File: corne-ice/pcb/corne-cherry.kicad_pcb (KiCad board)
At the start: 2 copper layers, 275.5 x 105.6 mm, 118 parts, among them J1 MJ-4PP-9, J2 OLED, J3 MJ-4PP-9, J4 OLED, SW1 SW_PUSH, SW10 SW_PUSH, SW11 SW_PUSH, SW12 SW_PUSH, SW13 SW_PUSH, SW14 SW_PUSH, SW15 SW_PUSH, SW16 SW_PUSH, SW17 SW_PUSH, SW18 SW_PUSH, SW19 SW_PUSH, SW2 SW_PUSH, SW20 SW_PUSH, SW21 SW_PUSH, SW22 SW_PUSH, SW23 SW_PUSH, SW24 SW_PUSH, SW25 SW_PUSH, SW26 SW_PUSH, SW27 SW_PUSH, SW28 SW_PUSH, SW29 SW_PUSH, SW3 SW_PUSH, SW30 SW_PUSH, SW31 SW_PUSH, SW32 SW_PUSH, SW33 SW_PUSH, SW34 SW_PUSH, SW35 SW_PUSH, SW36 SW_PUSH, SW37 SW_PUSH, SW38 SW_PUSH, SW39 SW_PUSH, SW4 SW_PUSH, SW40 SW_PUSH, SW41 SW_PUSH, SW42 SW_PUSH, SW5 SW_PUSH, SW6 SW_PUSH, SW7 SW_PUSH, SW8 SW_PUSH, SW9 SW_PUSH, U1 ProMicro, U2 ProMicro

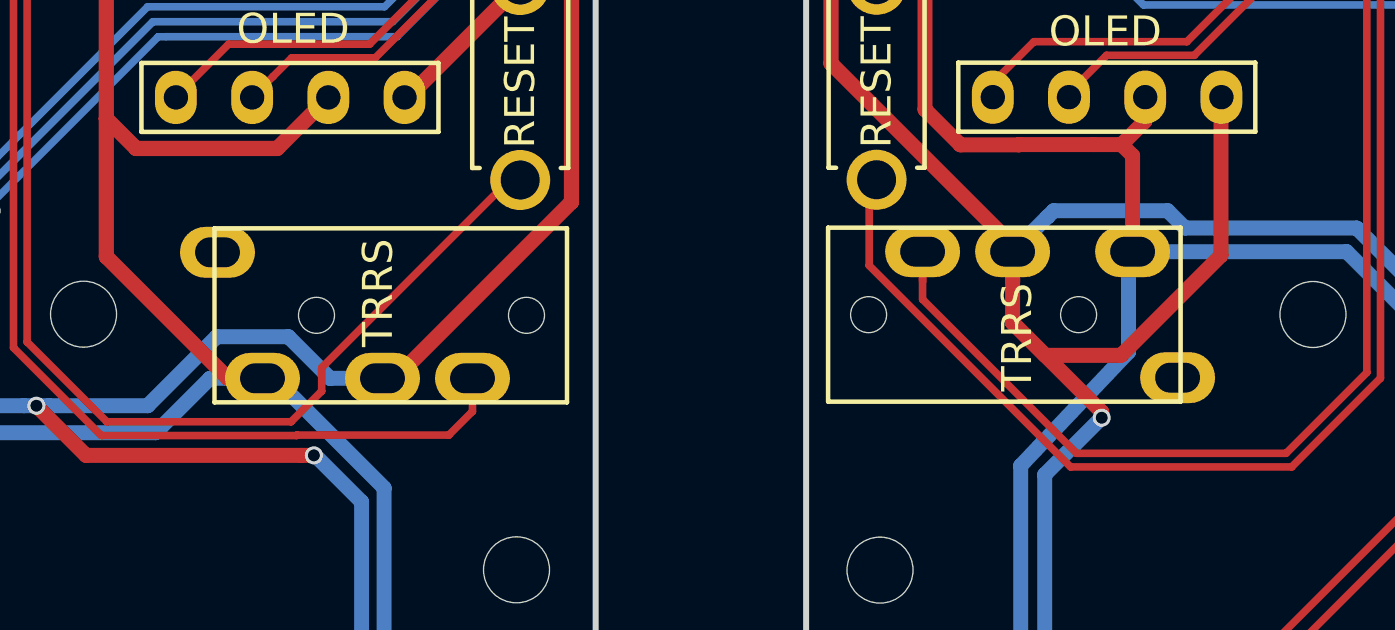
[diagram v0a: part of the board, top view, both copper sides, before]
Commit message: remove trrs
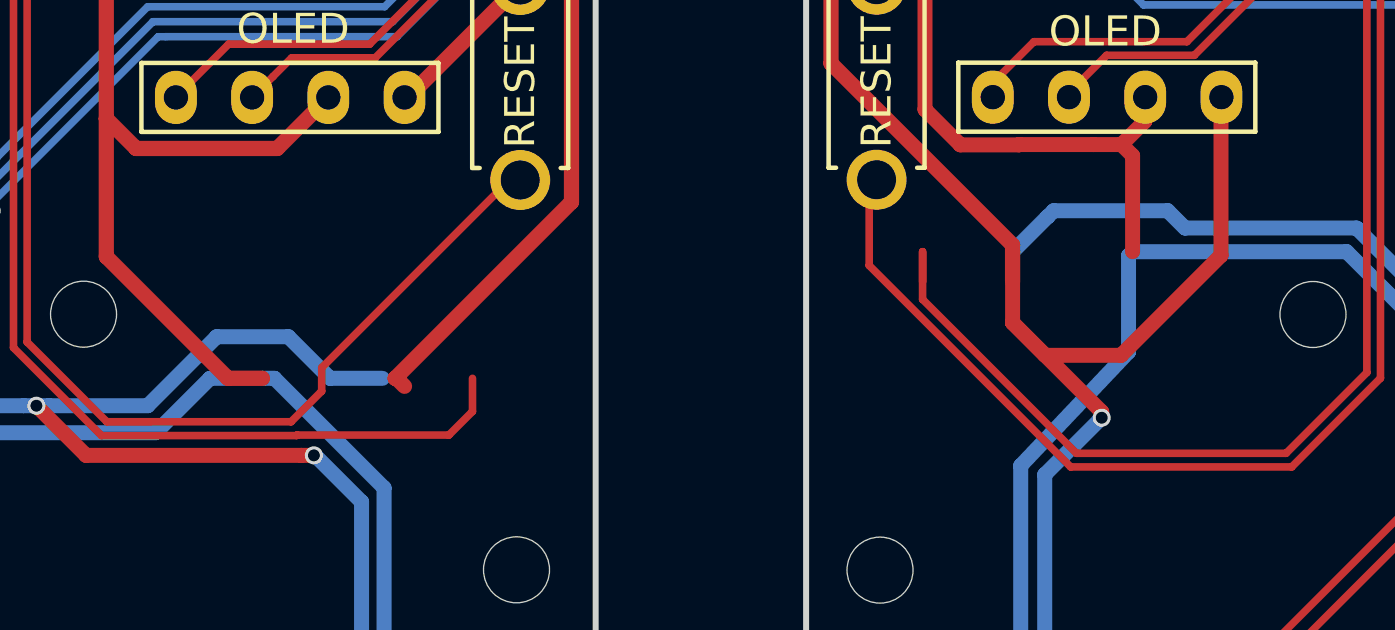
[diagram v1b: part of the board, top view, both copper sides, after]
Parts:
- removed J1, J3: MJ-4PP-9, kbd:MJ-4PP-9_1side
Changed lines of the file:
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@@
   (net 137 "Net-(U2-Pad14)")
   (net 138 "Net-(U2-Pad24)")
-  (net 139 "Net-(J1-PadA)")
-  (net 140 "Net-(J3-PadA)")
-  (footprint "kbd:MJ-4PP-9_1side" (layer "F.Cu")
-    (at 144.1345 74.292 -90)
-    (attr through_hole)
-    (fp_text reference "J1" (at -0.85 4.95 -90) (layer "F.Fab")
-      (effects (font (size 1 1) (thickness 0.15)))
-    )
-    (fp_text value "MJ-4PP-9" (at 0 14 -90) (layer "F.Fab") hide
-      (effects (font (size 1 1) (thickness 0.15)))
-    )
-    (fp_text user "TRRS" (at -0.75 6.45 -90) (layer "F.SilkS")
-      (effects (font (size 1 1) (thickness 0.15)))
-    )
-    (fp_line (start -2.9 0.15) (end 2.9 0.15) (layer "F.SilkS") (width 0.15))
-    (fp_line (start 2.9 0.15) (end 2.9 11.9) (layer "F.SilkS") (width 0.15))
-    (fp_line (start 2.9 11.9) (end -2.9 11.9) (layer "F.SilkS") (width 0.15))
-    (fp_line (start -2.9 11.9) (end -2.9 0.15) (layer "F.SilkS") (width 0.15))
-    (pad "" np_thru_hole circle locked (at 0 8.5 270) (size 1.2 1.2) (drill 1.2) (layers *.Cu *.Mask))
-    (pad "" np_thru_hole circle locked (at 0 1.5 270) (size 1.2 1.2) (drill 1.2) (layers *.Cu *.Mask))
-    (pad "A" thru_hole oval locked (at -2.1 11.8 270) (size 1.7 2.5) (drill oval 1 1.5) (layers *.Cu "B.Mask")
-      (net 139 "Net-(J1-PadA)") (clearance 0.15))
-    (pad "B" thru_hole oval locked (at 2.1 3.3 270) (size 1.7 2.5) (drill oval 1 1.5) (layers *.Cu "B.Mask")
-      (net 35 "data"))
-    (pad "C" thru_hole oval locked (at 2.1 6.3 270) (size 1.7 2.5) (drill oval 1 1.5) (layers *.Cu "B.Mask")
-      (net 26 "GND"))
-    (pad "D" thru_hole oval locked (at 2.1 10.3 270) (size 1.7 2.5) (drill oval 1 1.5) (layers *.Cu "B.Mask")
-      (net 27 "VCC") (clearance 0.15))
-    (model "/Users/foostan/src/github.com/foostan/kbd/kicad-packages3D/kbd.3dshapes/PJ320A.step"
-      (offset (xyz 0 -8.5 0))
-      (scale (xyz 1 1 1))
-      (rotate (xyz 0 0 0))
-    )
-  )
   (footprint "kbd:OLED_1side" (layer "F.Cu")
     (at 130.9485 67.028)
@@
     )
   )
-  (footprint "kbd:MJ-4PP-9_1side" (layer "F.Cu")
-    (at 152.5375 74.27 90)
-    (attr through_hole)
-    (fp_text reference "J3" (at -0.85 4.95 90) (layer "F.Fab")
-      (effects (font (size 1 1) (thickness 0.15)))
-    )
-    (fp_text value "MJ-4PP-9" (at 0 14 90) (layer "F.Fab") hide
-      (effects (font (size 1 1) (thickness 0.15)))
-    )
-    (fp_text user "TRRS" (at -0.75 6.45 90) (layer "F.SilkS")
-      (effects (font (size 1 1) (thickness 0.15)))
-    )
-    (fp_line (start 2.9 11.9) (end -2.9 11.9) (layer "F.SilkS") (width 0.15))
-    (fp_line (start -2.9 11.9) (end -2.9 0.15) (layer "F.SilkS") (width 0.15))
-    (fp_line (start -2.9 0.15) (end 2.9 0.15) (layer "F.SilkS") (width 0.15))
-    (fp_line (start 2.9 0.15) (end 2.9 11.9) (layer "F.SilkS") (width 0.15))
-    (pad "" np_thru_hole circle locked (at 0 8.5 90) (size 1.2 1.2) (drill 1.2) (layers *.Cu *.Mask))
-    (pad "" np_thru_hole circle locked (at 0 1.5 90) (size 1.2 1.2) (drill 1.2) (layers *.Cu *.Mask))
-    (pad "A" thru_hole oval locked (at -2.1 11.8 90) (size 1.7 2.5) (drill oval 1 1.5) (layers *.Cu "B.Mask")
-      (net 140 "Net-(J3-PadA)") (clearance 0.15))
-    (pad "B" thru_hole oval locked (at 2.1 3.3 90) (size 1.7 2.5) (drill oval 1 1.5) (layers *.Cu "B.Mask")
-      (net 69 "data_r"))
-    (pad "C" thru_hole oval locked (at 2.1 6.3 90) (size 1.7 2.5) (drill oval 1 1.5) (layers *.Cu "B.Mask")
-      (net 81 "GNDA"))
-    (pad "D" thru_hole oval locked (at 2.1 10.3 90) (size 1.7 2.5) (drill oval 1 1.5) (layers *.Cu "B.Mask")
-      (net 80 "VDD") (clearance 0.15))
-    (model "/Users/foostan/src/github.com/foostan/kbd/kicad-packages3D/kbd.3dshapes/PJ320A.step"
-      (offset (xyz 0 -8.5 0))
-      (scale (xyz 1 1 1))
-      (rotate (xyz 0 0 0))
-    )
-  )

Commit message: cleanup tracks
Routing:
- net GND: track 637.2 -> 49.9 mm, vias 16 -> 0
- net GNDA: track 617.9 -> 78.8 mm, vias 15 -> 0
- net VDD: track 573.1 -> 37.6 mm, vias 2 -> 0
- net VCC: track 544.3 -> 37.3 mm, vias 2 -> 0
- net data: track 77.0 -> 0.00 mm
- net Net-(LED31-Pad2): track 71.8 -> 0.00 mm, vias 2 -> 0
- net data_r: track 62.9 -> 0.00 mm
- net Net-(LED1-Pad4): track 47.8 -> 0.00 mm
- net Net-(LED32-Pad2): track 47.4 -> 0.00 mm
- net Net-(LED2-Pad4): track 46.3 -> 0.00 mm
- net Net-(LED4-Pad2): track 43.6 -> 0.00 mm, vias 2 -> 0
- net Net-(LED28-Pad2): track 41.5 -> 0.00 mm, vias 2 -> 0
- net LED: track 41.1 -> 0.00 mm
- net Net-(LED20-Pad4): track 36.8 -> 0.00 mm, vias 4 -> 0
- net Net-(LED29-Pad4): track 36.4 -> 0.00 mm
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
